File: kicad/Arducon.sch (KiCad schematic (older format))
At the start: 59 parts, among them J101 To Radio, J102 DB9 Female, J103 To Antenna, J104 Conn_01x08, J105 Conn_01x08, J106 Logic Level, J107 External Power Source, J108 Controlled Power, J109 Conn_01x01, J110 Conn_01x01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

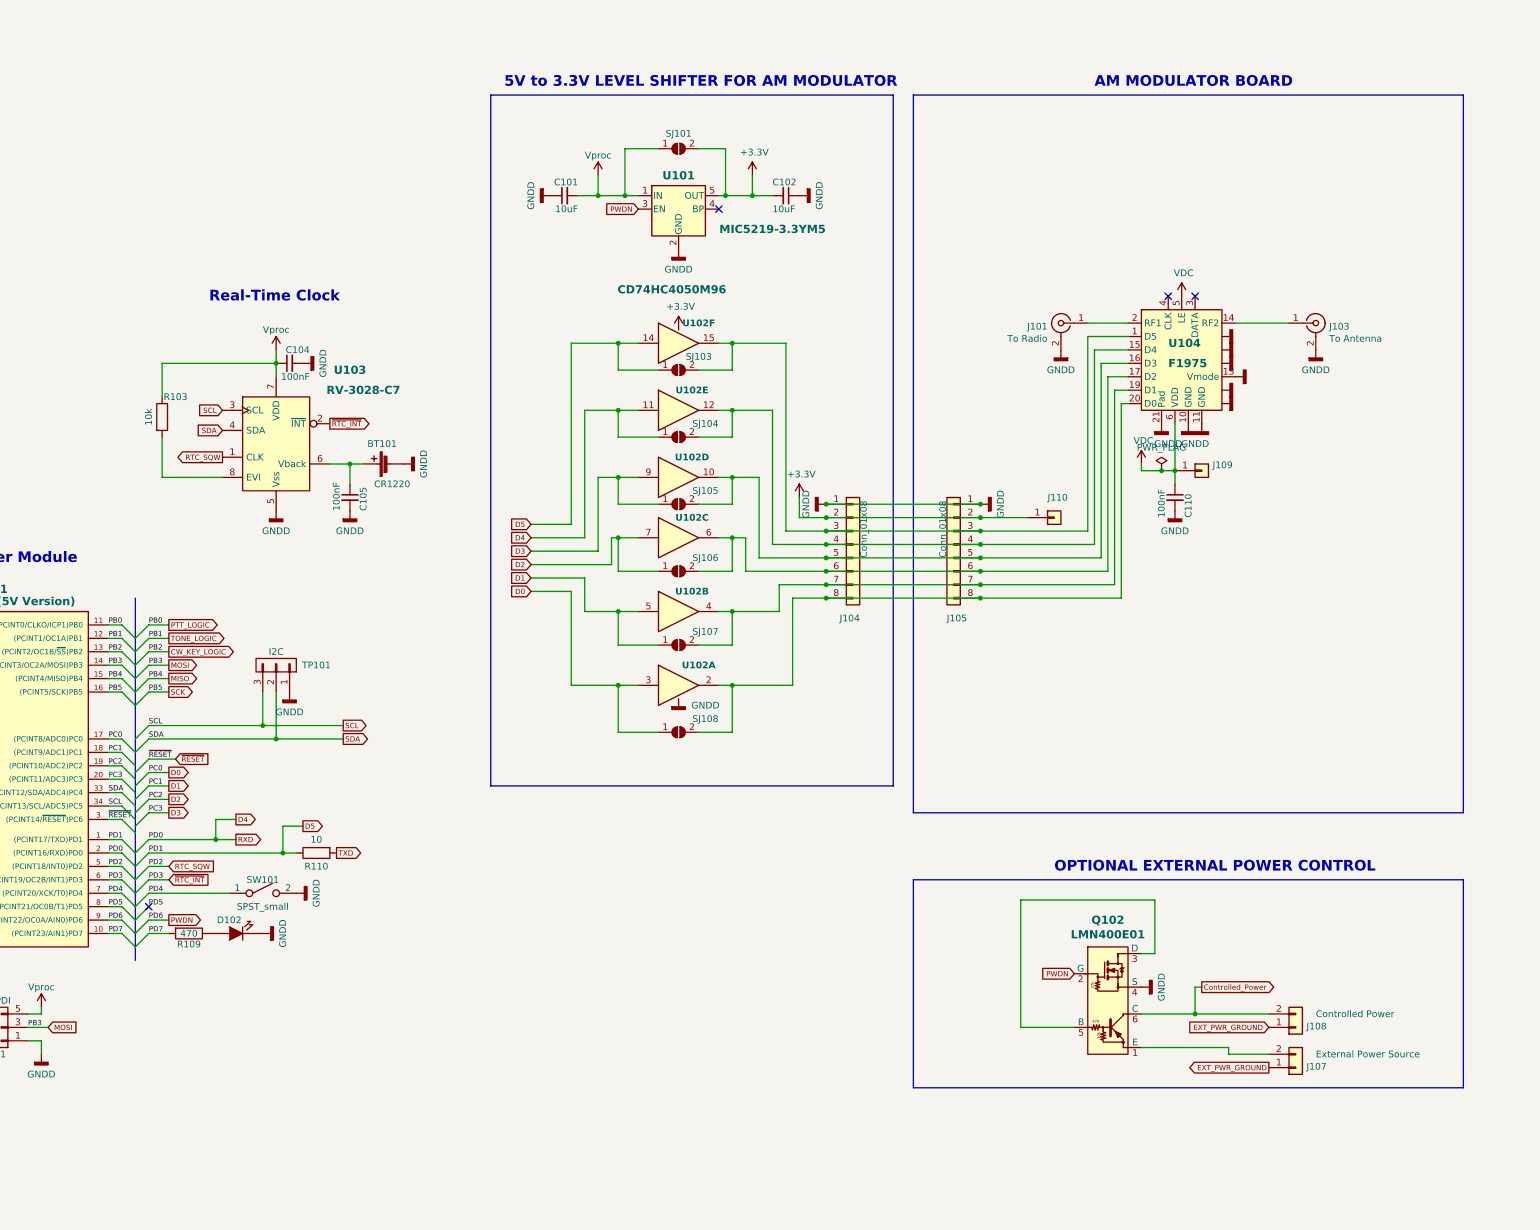
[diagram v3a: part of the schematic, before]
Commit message: RTC Stability
Added changes to keep Vcc noise from preventing the RTC from switching to backup battery power.
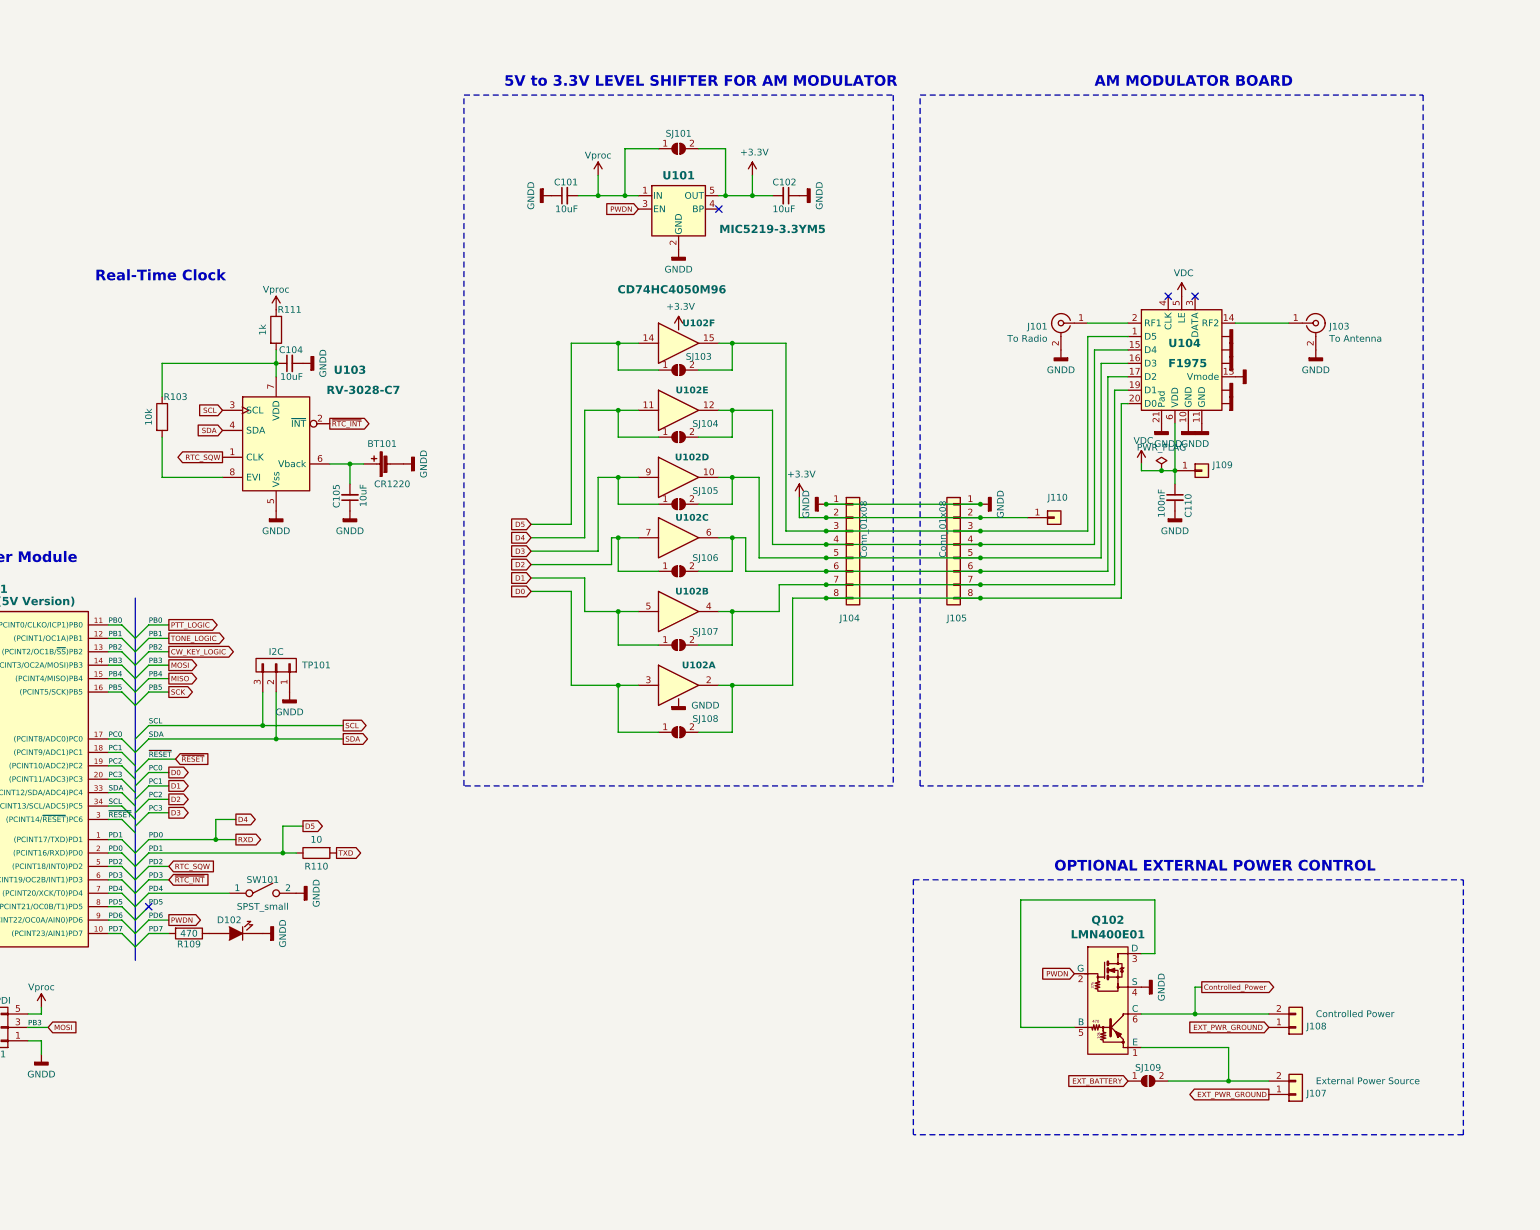
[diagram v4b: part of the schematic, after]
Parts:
- added R111: 1k, Resistors_SMD:R_0805, symbol Device:R
- added SJ109: SolderJumper_2_Open, Wire_Connections_Bridges:Solder-Jumper-NO-SMD-Pad_Small, symbol Jumper:SolderJumper_2_Open
- C104, C105: value 100nF -> 10uF; Link <a href=\"https://www.digikey.com/products/en?keywords=478-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 -> <a href=\"https://www.digikey.com/products/en?keywords=490-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; Part No. 478-1395-1-ND -> 490-5523-1-ND
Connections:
- net EXT_BATTERY: now also SJ109.1 (A)
- net GND: now also C105.1; no longer C105.2
- net Vproc: now also R111.1; no longer C104.1, R103.1, U103.7 (VDD)
- net at BT101.1, U103.6 (Vback): now also C105.2; no longer C105.1
- net at J107.2 (Pin_2), Q102.1 (E): now also SJ109.2 (B)
- new net: C104.1, R103.1, R111.2, U103.7 (VDD)
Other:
- moved on the sheet: J107
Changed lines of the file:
@@
 Text Label 5000 7800 2    39   ~ 0
 PB5
-Text Notes 6850 2400 0    79   ~ 16
+Text Notes 6000 2250 0    79   ~ 16
 Real-Time Clock
 Text Notes 12350 9500 0    118  ~ 24
@@
 L Arducon-rescue:Vproc #PWR0107
 U 1 1 5AB7DABB
-P 7350 2750
-F 0 "#PWR0107" H 7350 2600 50  0001 C CNN
-F 1 "Vproc" H 7350 2900 50  0000 C CNN
-F 2 "" H 7350 2750 50  0000 C CNN
-F 3 "" H 7350 2750 50  0000 C CNN
-	1    7350 2750
+P 7350 2450
+F 0 "#PWR0107" H 7350 2300 50  0001 C CNN
+F 1 "Vproc" H 7350 2600 50  0000 C CNN
+F 2 "" H 7350 2450 50  0000 C CNN
+F 3 "" H 7350 2450 50  0000 C CNN
+	1    7350 2450
 	1    0    0    -1
 $EndComp
@@
 Text GLabel 1800 4450 2    39   Input ~ 0
 PTT_LOGIC
-Text GLabel 14750 8100 0    39   Output ~ 0
+Text GLabel 14750 8300 0    39   Output ~ 0
 EXT_PWR_GROUND
 $Comp
@@
 Text GLabel 9250 4050 0    39   Input ~ 0
 D5
-Wire Bus Line
-	12100 6200 16200 6200
-Wire Bus Line
-	16200 6200 16200 850
-Wire Bus Line
-	16200 850  12100 850
-Wire Bus Line
-	12100 850  12100 6200
 $Comp
 L power:GNDD #PWR0123
@@
 Wire Wire Line
 	13800 7700 14200 7700
-Wire Bus Line
-	12100 6700 12100 8250
-Wire Bus Line
-	16200 8250 16200 6700
-Wire Bus Line
-	16200 6700 12100 6700
 Text Notes 13150 6650 0    79   ~ 16
 OPTIONAL EXTERNAL POWER CONTROL
@@
 $EndComp
 $Comp
-L Device:C_Small C104
-U 1 1 5FCCFFBE
-P 7450 2850
-F 0 "C104" V 7350 2700 50  0000 L CNN
-F 1 "100nF" V 7550 2700 50  0000 L CNN
-F 2 "Capacitors_SMD:C_0805" H 7450 2850 50  0001 C CNN
-F 3 "" H 7450 2850 50  0001 C CNN
-F 4 "478-1395-1-ND" H 7450 2850 60  0001 C CNN "Part No."
-F 5 "<a href=\"https://www.digikey.com/products/en?keywords=478-1395-1-ND\">Link</a>" H 7450 2850 60  0001 C CNN "Link"
-	1    7450 2850
-	0    -1   1    0
-$EndComp
-$Comp
 L Device:C_Small C109
 U 1 1 5FCD929C
@@
 	-1   0    0    -1
 $EndComp
-$Comp
-L Device:C_Small C105
-U 1 1 5FCE388F
-P 7900 3850
-F 0 "C105" V 7800 3750 50  0000 L CNN
-F 1 "100nF" V 8000 3750 50  0000 L CNN
-F 2 "Capacitors_SMD:C_0805" H 7900 3850 50  0001 C CNN
-F 3 "" H 7900 3850 50  0001 C CNN
-F 4 "478-1395-1-ND" H 7900 3850 60  0001 C CNN "Part No."
-F 5 "<a href=\"https://www.digikey.com/products/en?keywords=478-1395-1-ND\">Link</a>" H 7900 3850 60  0001 C CNN "Link"
-	1    7900 3850
-	-1   0    0    -1
-$EndComp
 Wire Wire Line
 	9550 2700 9900 2700
@@
 Text Notes 13450 800  0    79   ~ 16
 AM MODULATOR BOARD
-Wire Bus Line
-	8950 850  11950 850
-Wire Bus Line
-	11950 850  11950 6000
-Wire Bus Line
-	11950 6000 8950 6000
-Wire Bus Line
-	8950 6000 8950 850
 Text Notes 9050 800  0    79   ~ 16
 5V to 3.3V LEVEL SHIFTER FOR AM MODULATOR
@@
 L Connector_Generic:Conn_01x02 J107
 U 1 1 5FE800D7
-P 14950 8100
-F 0 "J107" H 15030 8092 50  0000 L CNN
-F 1 "External Power Source" H 15100 8000 50  0000 L CNN
-F 2 "Wire_Pads:SolderWirePad_2x_1-5mmDrill_Polarized" H 14950 8100 50  0001 C CNN
-F 3 "" H 14950 8100 50  0001 C CNN
-F 4 "np" H 14950 8100 50  0001 C CNN "Part No."
-F 5 "np" H 14950 8100 50  0001 C CNN "Link"
-	1    14950 8100
+P 14950 8300
+F 0 "J107" H 15030 8292 50  0000 L CNN
+F 1 "External Power Source" H 15100 8200 50  0000 L CNN
+F 2 "Wire_Pads:SolderWirePad_2x_1-5mmDrill_Polarized" H 14950 8300 50  0001 C CNN
+F 3 "" H 14950 8300 50  0001 C CNN
+F 4 "np" H 14950 8300 50  0001 C CNN "Part No."
+F 5 "np" H 14950 8300 50  0001 C CNN "Link"
+	1    14950 8300
 	1    0    0    1
 $EndComp
@@
 Text GLabel 10050 1700 0    39   Input ~ 0
 PWDN
-Wire Bus Line
-	12100 8250 16200 8250
 Wire Wire Line
 	13800 7950 14450 7950
 Wire Wire Line
-	14450 7950 14450 8000
-Wire Wire Line
-	14450 8000 14750 8000
+	14450 7950 14450 8200
+Wire Wire Line
+	14450 8200 14750 8200
+Text GLabel 13700 8200 0    39   Input ~ 0
+EXT_BATTERY
+$Comp
+L Jumper:SolderJumper_2_Open SJ109
+U 1 1 5FEA63C0
+P 13850 8200
+F 0 "SJ109" H 13850 8300 50  0000 C CNN
+F 1 "SolderJumper_2_Open" H 13850 8314 50  0001 C CNN
+F 2 "Wire_Connections_Bridges:Solder-Jumper-NO-SMD-Pad_Small" H 13850 8200 50  0001 C CNN
+F 3 "" H 13850 8200 50  0001 C CNN
+F 4 "np" H 13850 8200 50  0001 C CNN "Part No."
+F 5 "np" H 13850 8200 50  0001 C CNN "Link"
+	1    13850 8200
+	1    0    0    -1
+$EndComp
+Wire Wire Line
+	14000 8200 14450 8200
+Connection ~ 14450 8200
+Wire Notes Line
+	12100 6700 16200 6700
+Wire Notes Line
+	16200 6700 16200 8600
+Wire Notes Line
+	16200 8600 12100 8600
+Wire Notes Line
+	12100 8600 12100 6700
+Wire Notes Line
+	8750 850  11950 850
+Wire Notes Line
+	11950 850  11950 6000
+Wire Notes Line
+	11950 6000 8750 6000
+Wire Notes Line
+	8750 6000 8750 850
+Wire Notes Line
+	12150 850  15900 850
+Wire Notes Line
+	15900 850  15900 6000
+Wire Notes Line
+	15900 6000 12150 6000
+Wire Notes Line
+	12150 6000 12150 850
+$Comp
+L Device:R R111
+U 1 1 600A7372
+P 7350 2600
+F 0 "R111" H 7450 2750 50  0000 C CNN
+F 1 "1k" V 7250 2600 50  0000 C CNN
+F 2 "Resistors_SMD:R_0805" H 7280 2600 50  0001 C CNN
+F 3 "" H 7350 2600 50  0001 C CNN
+F 4 "311-1.00KCRCT-ND" H 7350 2600 60  0001 C CNN "Part No."
+F 5 "<a href=\"https://www.digikey.com/products/en?keywords=311-1.00KCRCT-ND\">Link</a>" H 7350 2600 60  0001 C CNN "Link"
+	1    7350 2600
+	1    0    0    -1
+$EndComp
+$Comp
+L Device:C_Small C104
+U 1 1 60097870
+P 7450 2850
+F 0 "C104" V 7550 2750 50  0000 L CNN
+F 1 "10uF" V 7350 2750 50  0000 L CNN
+F 2 "Capacitors_SMD:C_0805" H 7450 2850 50  0001 C CNN
+F 3 "http://www.kemet.com/Lists/ProductCatalog/Attachments/53/KEM_C1002_X7R_SMD.pdf" H 7450 2850 50  0001 C CNN
+F 4 "490-5523-1-ND" H 7450 2850 60  0001 C CNN "Part No."
+F 5 "<a href=\"https://www.digikey.com/products/en?keywords=490-5523-1-ND\">Link</a>" H 7450 2850 60  0001 C CNN "Link"
+	1    7450 2850
+	0    -1   -1   0
+$EndComp
+$Comp
+L Device:C_Small C105
+U 1 1 600ABBF4
+P 7900 3850
+F 0 "C105" V 8000 3750 50  0000 L CNN
+F 1 "10uF" V 7800 3750 50  0000 L CNN
+F 2 "Capacitors_SMD:C_0805" H 7900 3850 50  0001 C CNN
+F 3 "http://www.kemet.com/Lists/ProductCatalog/Attachments/53/KEM_C1002_X7R_SMD.pdf" H 7900 3850 50  0001 C CNN
+F 4 "490-5523-1-ND" H 7900 3850 60  0001 C CNN "Part No."
+F 5 "<a href=\"https://www.digikey.com/products/en?keywords=490-5523-1-ND\">Link</a>" H 7900 3850 60  0001 C CNN "Link"
+	1    7900 3850
+	-1   0    0    1
+$EndComp
 Wire Bus Line
 	6300 4600 6300 7300

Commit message: ESD diode footprints
Changed ESD diode footprints to 0603
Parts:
- D103, D104, D105, D106, D107: footprint Diodes_SMD:SOD-923 -> Resistors_SMD:R_0603
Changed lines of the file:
@@
 F 0 "D103" H 2150 8121 50  0000 R CNN
 F 1 "ESD9B5.0ST5G" V 2105 8121 50  0001 R CNN
-F 2 "Diodes_SMD:SOD-923" H 2150 8200 50  0001 C CNN
+F 2 "Resistors_SMD:R_0603" H 2150 8200 50  0001 C CNN
 F 3 "https://www.onsemi.com/pub/Collateral/ESD9B-D.PDF" H 2150 8200 50  0001 C CNN
 F 4 "ESD9B5.0ST5GOSCT-ND" H 2150 8200 50  0001 C CNN "Part No."
@@
 F 0 "D104" H 2400 8121 50  0000 R CNN
 F 1 "ESD9B5.0ST5G" V 2355 8121 50  0001 R CNN
-F 2 "Diodes_SMD:SOD-923" H 2400 8200 50  0001 C CNN
+F 2 "Resistors_SMD:R_0603" H 2400 8200 50  0001 C CNN
 F 3 "https://www.onsemi.com/pub/Collateral/ESD9B-D.PDF" H 2400 8200 50  0001 C CNN
 F 4 "ESD9B5.0ST5GOSCT-ND" H 2400 8200 50  0001 C CNN "Part No."
@@
 F 0 "D105" H 2650 8121 50  0000 R CNN
 F 1 "ESD9B5.0ST5G" V 2605 8121 50  0001 R CNN
-F 2 "Diodes_SMD:SOD-923" H 2650 8200 50  0001 C CNN
+F 2 "Resistors_SMD:R_0603" H 2650 8200 50  0001 C CNN
 F 3 "https://www.onsemi.com/pub/Collateral/ESD9B-D.PDF" H 2650 8200 50  0001 C CNN
 F 4 "ESD9B5.0ST5GOSCT-ND" H 2650 8200 50  0001 C CNN "Part No."
@@
 F 0 "D106" H 2900 8121 50  0000 R CNN
 F 1 "ESD9B5.0ST5G" V 2855 8121 50  0001 R CNN
-F 2 "Diodes_SMD:SOD-923" H 2900 8200 50  0001 C CNN
+F 2 "Resistors_SMD:R_0603" H 2900 8200 50  0001 C CNN
 F 3 "https://www.onsemi.com/pub/Collateral/ESD9B-D.PDF" H 2900 8200 50  0001 C CNN
 F 4 "ESD9B5.0ST5GOSCT-ND" H 2900 8200 50  0001 C CNN "Part No."
@@
 F 0 "D107" H 3150 8121 50  0000 R CNN
 F 1 "ESD9B5.0ST5G" V 3105 8121 50  0001 R CNN
-F 2 "Diodes_SMD:SOD-923" H 3150 8200 50  0001 C CNN
+F 2 "Resistors_SMD:R_0603" H 3150 8200 50  0001 C CNN
 F 3 "https://www.onsemi.com/pub/Collateral/ESD9B-D.PDF" H 3150 8200 50  0001 C CNN
 F 4 "ESD9B5.0ST5GOSCT-ND" H 3150 8200 50  0001 C CNN "Part No."
